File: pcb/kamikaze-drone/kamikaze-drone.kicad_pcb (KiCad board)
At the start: 4 copper layers, 50 x 50 mm, 88 parts, among them M1 Brushless DC, M2 Brushless DC, M3 Brushless DC, M4 Brushless DC, Q1 SI2300DS, Q2 SI2300DS, Q3 SI2300DS, Q4 SI2300DS, U1 STM32F765VITx, U2 USBLC6-2P6, U3 MCP73871-2CC, U4 AMS1117-3.3, U5 LSM6DSL, U6 W25Q64JVSS, U7 BMP280, U8 VL53L1CXV0FY1

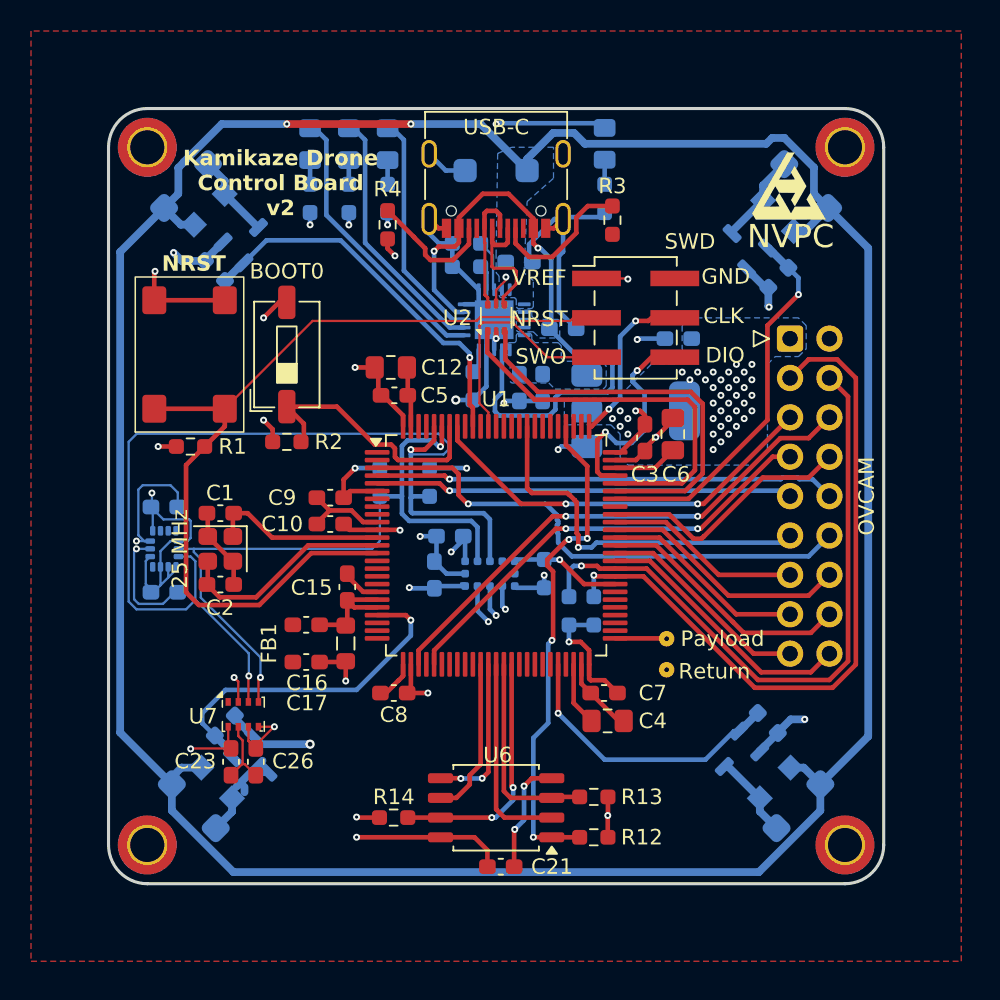
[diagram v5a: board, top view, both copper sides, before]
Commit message: feat: added touch points to PCB
Took advice from reddit to improve the PCB schematic
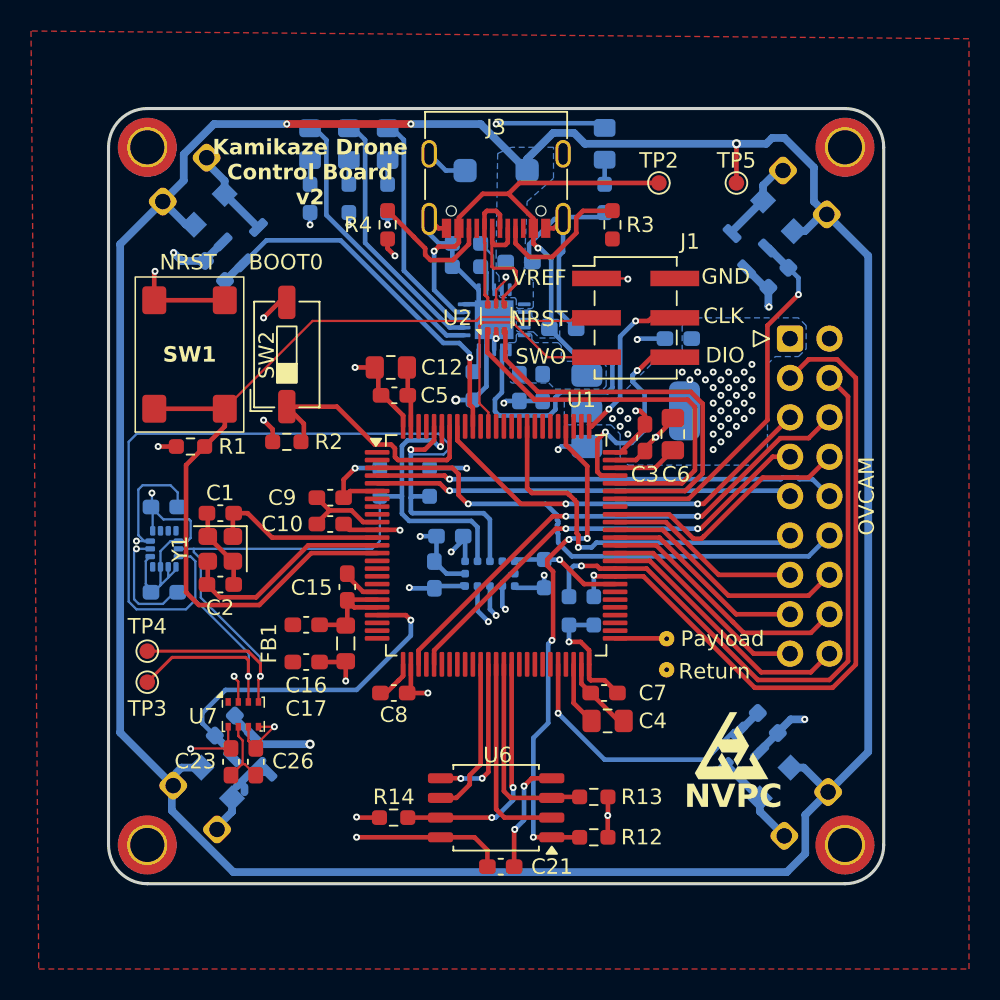
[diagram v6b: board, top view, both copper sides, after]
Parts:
- added TP2: TestPoint, TestPoint:TestPoint_Pad_D1.0mm, F.Cu at (160.5, 79.8)
- added TP3: TestPoint, TestPoint:TestPoint_Pad_D1.0mm, F.Cu at (127.5, 112.0)
- added TP4: TestPoint, TestPoint:TestPoint_Pad_D1.0mm, F.Cu at (127.5, 110.0)
- added TP5: TestPoint, TestPoint:TestPoint_Pad_D1.0mm, F.Cu at (165.5, 79.8)
- Y1: renamed from 25 MHz
- moved NVPC 36.3 mm to (165.3, 116.1)
- moved M4 0.71 mm to (170.0, 120.5)
- moved M1 0.42 mm to (129.9, 79.6)
- moved M2 0.42 mm to (169.9, 80.4)
- moved R3 0.30 mm to (157.5, 82.5)
- moved M3 0.12 mm to (130.6, 120.1)
- renumbered SWD to J1, Battery to J2, USB-C to J3, NRST to SW1, BOOT0 to SW2
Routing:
- net VBUS: track 42.0 -> 52.0 mm
- net I2C1_SCL: track 45.2 -> 53.6 mm
- net I2C1_SDA: track 66.5 -> 74.8 mm
- net VBAT: track 189.2 -> 193.6 mm, vias 2 -> 3
- net +3V3: track 104.7 -> 104.8 mm, vias 64 -> 63
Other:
- board text added: "BOOT0"

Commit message: v3 of PCB made. ov7670 implementation guide added
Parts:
- M1, M2, M3, M4: value Brushless DC -> DC Motor
- renumbered Payload to H5, Return to H6, OVCAM to J4
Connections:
- U2 pad 5: +3V3 -> VBUS
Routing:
- net VBUS: track 52.0 -> 57.4 mm, vias 2 -> 3
- net VBAT: track 193.6 -> 195.5 mm
- net +3V3: track 104.8 -> 102.9 mm, vias 63 -> 62
- net USBR_D+: track 8.03 -> 9.58 mm
- added copper zone on B.Cu, net GND
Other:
- board text added: "Kamikaze Drone Control Board v3"
- board text added: "M1"
- board text added: "M2"
- board text added: "M3"
- board text added: "M4"
- board text removed: "Kamikaze Drone Control Board v2"

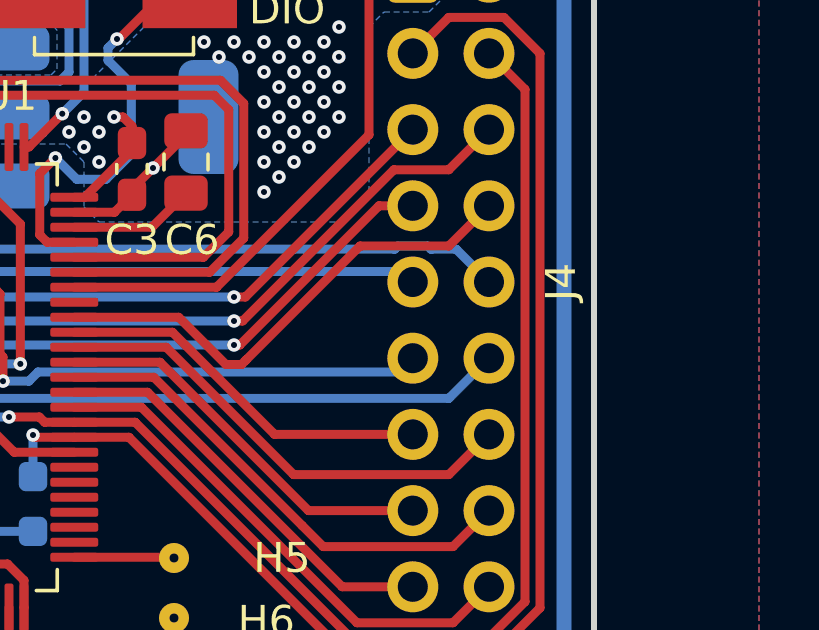
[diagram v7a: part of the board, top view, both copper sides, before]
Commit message: firmware: added ov7670 camera support and updated gitignore
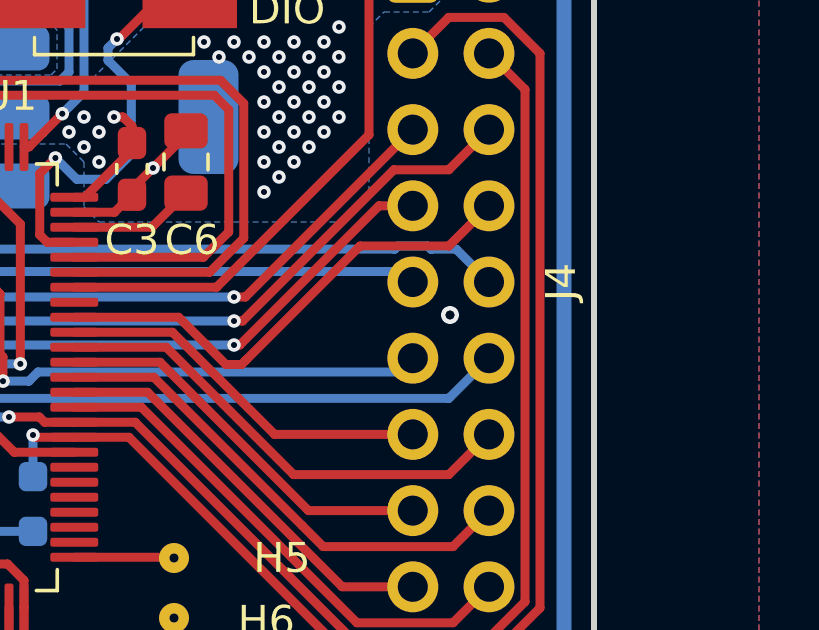
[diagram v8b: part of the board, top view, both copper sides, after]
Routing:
- net GND: vias 21 -> 22
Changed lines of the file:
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@@
 	)
 	(via
+		(at 170.2 101.1)
+		(size 0.6)
+		(drill 0.3)
+		(layers "F.Cu" "B.Cu")
+		(free yes)
+		(net 2)
+	)
+	(via
 		(at 147.4 93.8)
 		(size 0.6)
@@
 			(thermal_gap 0.5)
 			(thermal_bridge_width 0.5)
+			(island_removal_mode 1)
+			(island_area_min 10)
 		)
 		(polygon
